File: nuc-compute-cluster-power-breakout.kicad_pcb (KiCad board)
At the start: 4 copper layers, 100 x 100 mm, 112 parts, among them J1 USB3106-30-0230-A, J2 BM04B-SRSS-TB-LF-SN, J3 BM04B-SRSS-TB-LF-SN, J4 43045-1013, J5 430450812, J6 430450812, J7 430450812, J8 430450812, J9 430450812, Q1 SQS401EN-T1_BE3, Q10 SSM3K15ACT, Q2 SQS401EN-T1_BE3, Q3 SSM3K15ACT, Q4 SSM3K15ACT, Q5 SQS401EN-T1_BE3, Q6 SSM3K15ACT, Q7 SQS401EN-T1_BE3, Q8 SQS401EN-T1_BE3, Q9 SSM3K15ACT, U1 FT2232HL-REEL, U10 TCA9534, U11 TMCS1100A2-Q1, U12 TMCS1100A2-Q1, U13 TMCS1100A2-Q1, U14 ADS7828, U15 AP62301WU-7, U7 AP62301WU-7, U8 TMCS1100A2-Q1, U9 TMCS1100A2-Q1, Y1 KX-7_12,MHz

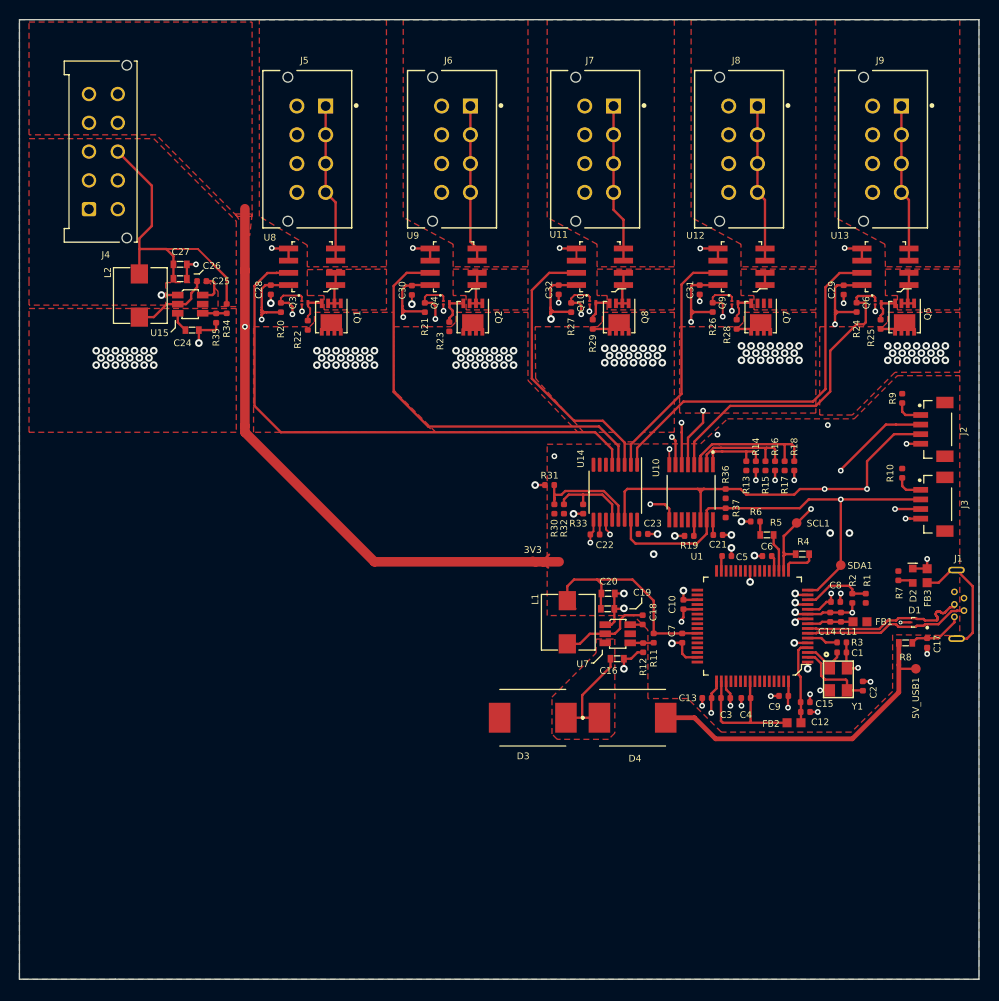
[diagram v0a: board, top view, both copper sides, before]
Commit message: Power planes alignment
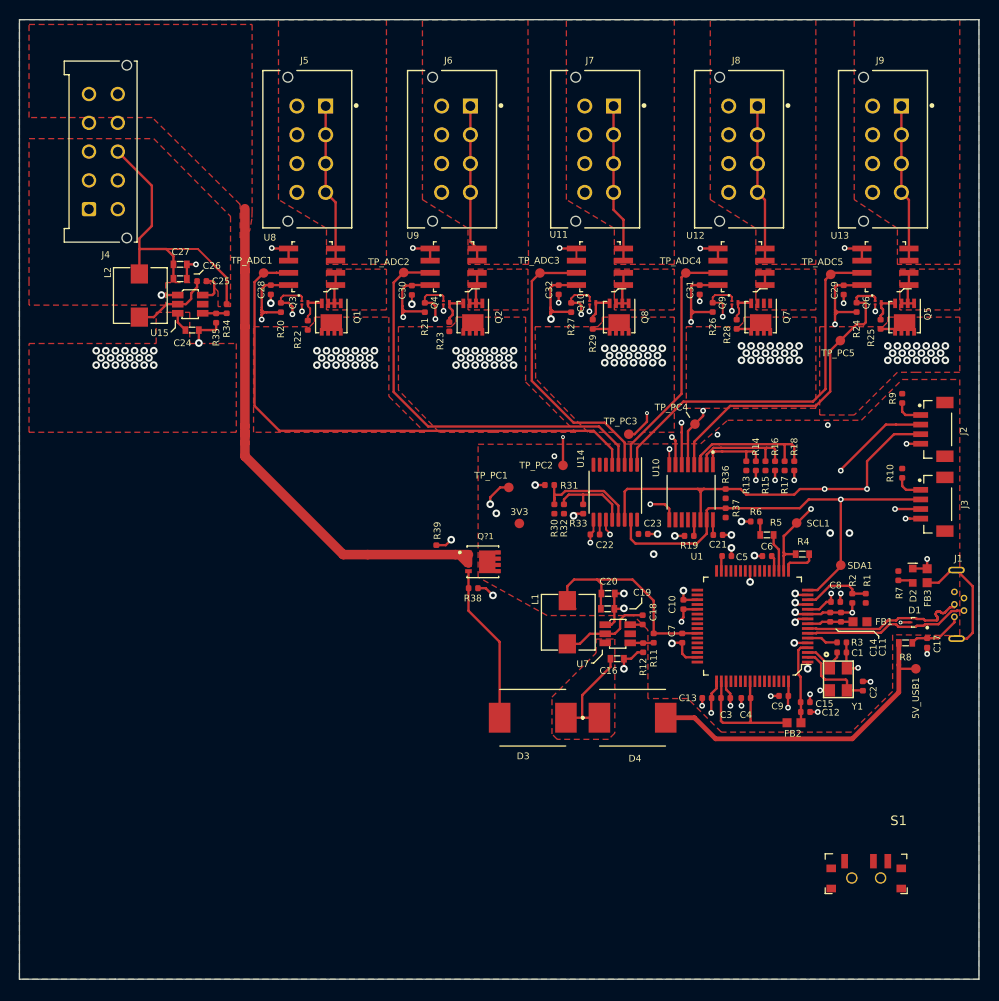
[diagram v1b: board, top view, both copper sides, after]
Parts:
- added Q?1: DMN4010LFG-7, antmicro-footprints:POWERVDFN-8, F.Cu at (138.3, 106.5)
- added R38: R_10k_0402, antmicro-footprints:0402-res, F.Cu at (137.3, 109.2)
- added R39: R_10k_0402, antmicro-footprints:0402-res, F.Cu at (133.4, 105.2)
- added S1: MSS3-V-T_R, antmicro-footprints:Switch_Slide_MSS3, F.Cu at (178.2, 139.4)
- added TP_ADC1: TP_SMD1MM, antmicro-footprints:Testpoint_smd_1mm, F.Cu at (115.5, 76.5)
- added TP_ADC2: TP_SMD1MM, antmicro-footprints:Testpoint_smd_1mm, F.Cu at (130.1, 76.4)
- added TP_ADC3: TP_SMD1MM, antmicro-footprints:Testpoint_smd_1mm, F.Cu at (144.2, 76.5)
- added TP_ADC4: TP_SMD1MM, antmicro-footprints:Testpoint_smd_1mm, F.Cu at (159.4, 76.5)
- added TP_ADC5: TP_SMD1MM, antmicro-footprints:Testpoint_smd_1mm, F.Cu at (174.6, 76.6)
- added TP_PC1: TP_SMD1MM, antmicro-footprints:Testpoint_smd_1mm, F.Cu at (141.0, 98.8)
- added TP_PC2: TP_SMD1MM, antmicro-footprints:Testpoint_smd_1mm, F.Cu at (146.7, 96.5)
- added TP_PC3: TP_SMD1MM, antmicro-footprints:Testpoint_smd_1mm, F.Cu at (153.5, 93.3)
- added TP_PC4: TP_SMD1MM, antmicro-footprints:Testpoint_smd_1mm, F.Cu at (160.4, 92.2)
- added TP_PC5: TP_SMD1MM, antmicro-footprints:Testpoint_smd_1mm, F.Cu at (175.6, 83.5)
- moved 3V3 4.19 mm to (142.1, 102.6)
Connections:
- J1 pad 4: (no net) -> Net-(J1-Pad4)
- J4 pad 10: VCC3V3 -> DB_3V3
- J4 pad 5: VCC3V3 -> DB_3V3
- U1 pad 21: (no net) -> Net-(U1-Pad21)
- U1 pad 22: (no net) -> Net-(U1-Pad22)
- U1 pad 23: (no net) -> Net-(U1-Pad23)
- U1 pad 24: (no net) -> Net-(U1-Pad24)
- U1 pad 26: (no net) -> Net-(U1-Pad26)
- U1 pad 27: (no net) -> Net-(U1-Pad27)
- U1 pad 28: (no net) -> Net-(U1-Pad28)
- U1 pad 29: (no net) -> Net-(U1-Pad29)
- U1 pad 30: (no net) -> Net-(U1-Pad30)
- U1 pad 32: (no net) -> Net-(U1-Pad32)
- U1 pad 33: (no net) -> Net-(U1-Pad33)
- U1 pad 34: (no net) -> Net-(U1-Pad34)
- U1 pad 36: (no net) -> Net-(U1-Pad36)
- U1 pad 38: (no net) -> Net-(U1-Pad38)
- U1 pad 39: (no net) -> Net-(U1-Pad39)
- U1 pad 40: (no net) -> Net-(U1-Pad40)
- U1 pad 41: (no net) -> Net-(U1-Pad41)
- U1 pad 43: (no net) -> Net-(U1-Pad43)
- U1 pad 44: (no net) -> Net-(U1-Pad44)
- U1 pad 45: (no net) -> Net-(U1-Pad45)
- U1 pad 46: (no net) -> Net-(U1-Pad46)
- U1 pad 48: (no net) -> Net-(U1-Pad48)
- U1 pad 52: (no net) -> Net-(U1-Pad52)
- U1 pad 53: (no net) -> Net-(U1-Pad53)
- U1 pad 54: (no net) -> Net-(U1-Pad54)
- U1 pad 55: (no net) -> Net-(U1-Pad55)
- U1 pad 57: (no net) -> Net-(U1-Pad57)
- U1 pad 58: (no net) -> Net-(U1-Pad58)
- U1 pad 59: (no net) -> Net-(U1-Pad59)
- U1 pad 60: (no net) -> Net-(U1-Pad60)
- U1 pad 61: (no net) -> Net-(U1-Pad61)
- U1 pad 62: (no net) -> Net-(U1-Pad62)
- U1 pad 63: (no net) -> Net-(U1-Pad63)
- U10 pad 10: (no net) -> Net-(U10-Pad10)
- U10 pad 11: (no net) -> Net-(U10-Pad11)
- U10 pad 12: (no net) -> Net-(U10-Pad12)
- U14 pad 6: (no net) -> Net-(U14-Pad6)
- U14 pad 7: (no net) -> Net-(U14-Pad7)
- U14 pad 8: (no net) -> Net-(U14-Pad8)
- U15 pad 5: (no net) -> Net-(U15-Pad5)
- U7 pad 5: (no net) -> Net-(U7-Pad5)
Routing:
- net DB_3V3: track 0.00 -> 59.0 mm
- net VCC3V3: track 237.4 -> 209.4 mm
- net VCC12V0: track 11.3 -> 27.9 mm
- net /Power Cycling & Current Measurement/PC_1: track 63.8 -> 67.7 mm, vias 2 -> 3
- net GND: track 98.5 -> 102.2 mm, vias 59 -> 61
- net /Power Cycling & Current Measurement/PC_3: track 27.5 -> 31.0 mm, vias 2 -> 3
- net /Power Cycling & Current Measurement/PC_2: track 43.2 -> 46.1 mm, vias 2 -> 3
- net /Power Cycling & Current Measurement/C_ADC3: track 29.4 -> 30.1 mm
- added copper zone on F.Cu, net DB_3V3
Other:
- board text removed: "TODO: Improve layout of Hall-effect current Sensors ( p.39 of the datasheet)"
- board text removed: "TODO: unify the font - Use EDIT --> Edit text and graphical properties"

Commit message: Replaced +3V3 with GND plane
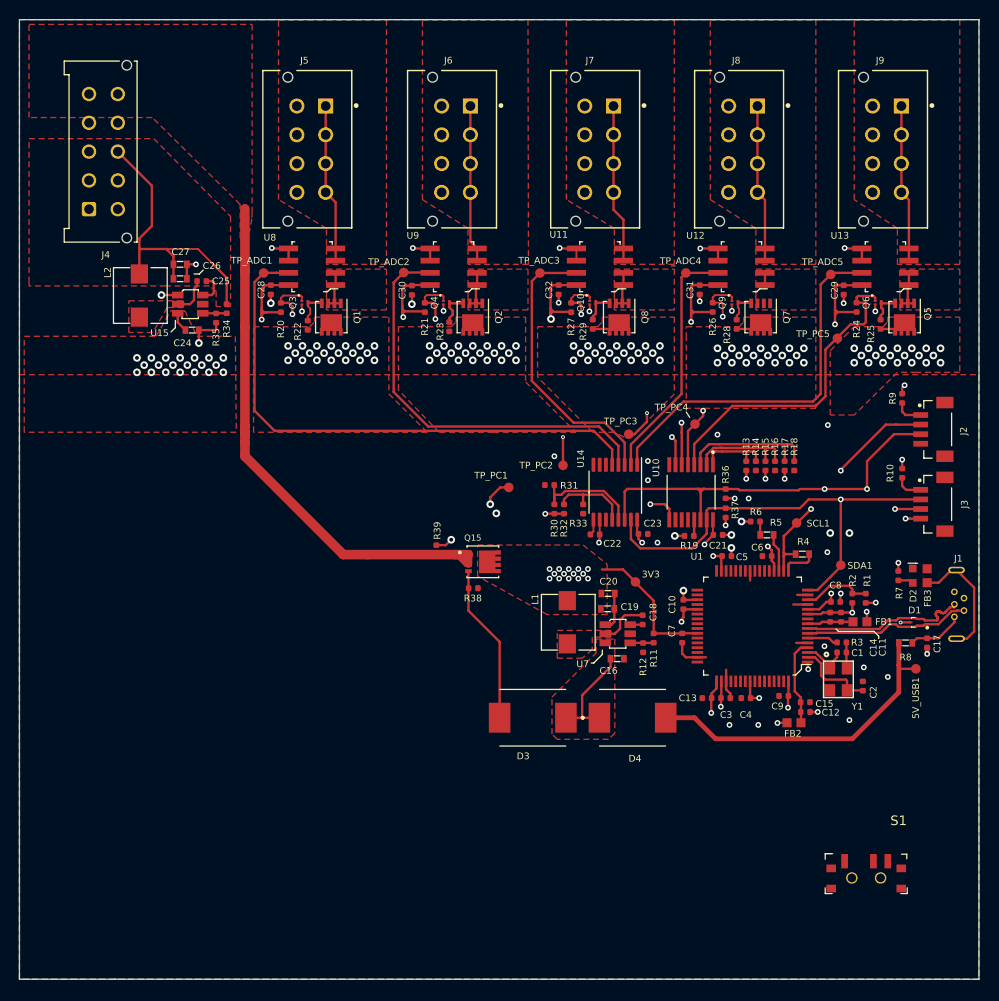
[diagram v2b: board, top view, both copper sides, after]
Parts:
- moved 3V3 13.6 mm to (154.2, 108.7)
- moved TP_PC5 0.39 mm to (175.2, 83.2)
- renumbered Q?1 to Q15
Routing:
- net GND: track 102.2 -> 70.4 mm, vias 61 -> 41
- net Net-(C18-Pad1): track 9.61 -> 5.23 mm
- net Net-(C25-Pad1): track 8.29 -> 3.98 mm
- net /Power Cycling & Current Measurement/PC_2: track 46.1 -> 49.9 mm
- net /Power Cycling & Current Measurement/PC_3: track 31.0 -> 34.8 mm
- net VCC3V3: track 209.4 -> 208.4 mm, vias 13 -> 45
- added copper zone on F.Cu, net GND
- added copper zone on F.Cu, net Net-(C18-Pad1)
- added copper zone on F.Cu, net Net-(C25-Pad1)
- added copper zone on In2.Cu, net VCC3V3
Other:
- board text removed: "TODO: Fix unequal planes distribution (TOP) -Manufacturers always require equal planes distribution on each layer."
- board text removed: "TODO: Improve layout of Net-(C18-Pad1) trace"
- board text removed: "TODO: Improve layout of Net-(C25-Pad1) trace"
- board text removed: "TODO: Increase clereances between the power planes"
- board text removed: "TODO: Move 3V3 power plane to inner layer. - Add GND plane instead"

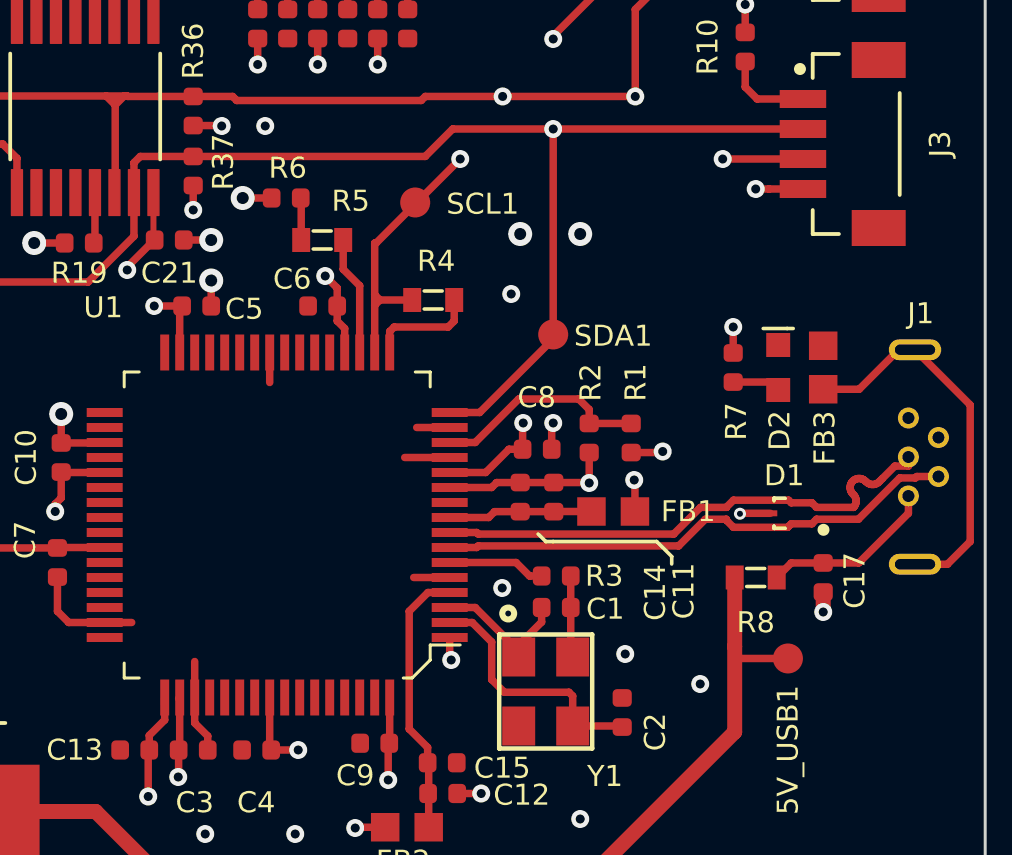
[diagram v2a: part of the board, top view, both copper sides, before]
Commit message: FTDI layout redesign
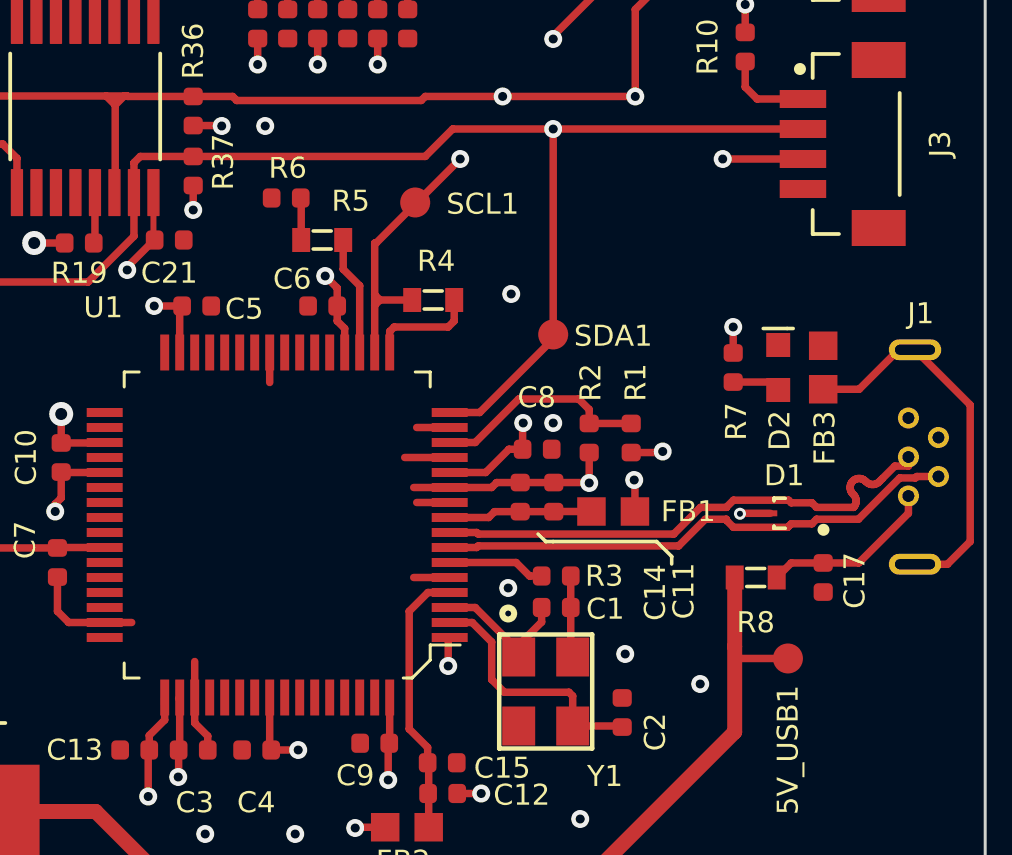
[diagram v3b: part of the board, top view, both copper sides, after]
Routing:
- net GND: track 70.4 -> 67.3 mm, vias 41 -> 36
- net VCC3V3: track 208.4 -> 206.4 mm, vias 45 -> 43
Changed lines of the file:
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@@
     (thickness 1.6)
     (drawings 22)
-    (tracks 1035)
+    (tracks 1022)
     (zones 0)
     (modules 126)
@@
   (segment (start 160.5 92) (end 160.5 93.25) (width 0.25) (layer In2.Cu) (net 1))
   (segment (start 162.75 93.25) (end 160.5 93.25) (width 0.25) (layer In2.Cu) (net 1))
-  (via (at 174.5 103.5) (size 0.8) (drill 0.4) (layers F.Cu B.Cu) (net 1))
-  (via (at 176.5 103.5) (size 0.8) (drill 0.4) (layers F.Cu B.Cu) (net 1))
-  (segment (start 174.5 103.5) (end 176.5 103.5) (width 0.5) (layer In2.Cu) (net 1))
   (segment (start 115.25 90.783172) (end 115.25 81.25) (width 0.25) (layer In2.Cu) (net 1))
   (segment (start 125.866828 101.4) (end 115.25 90.783172) (width 0.25) (layer In2.Cu) (net 1))
@@
   (segment (start 160.635 110.465) (end 160.65 110.45) (width 0.25) (layer F.Cu) (net 4))
   (segment (start 159.2 110.465) (end 160.635 110.465) (width 0.25) (layer F.Cu) (net 4))
-  (via (at 184.6 116.1) (size 0.6) (drill 0.3) (layers F.Cu B.Cu) (net 4))
-  (segment (start 184.6 115.435) (end 184.6 115.9) (width 0.5) (layer F.Cu) (net 4))
   (via (at 176.8 111.8) (size 0.6) (drill 0.3) (layers F.Cu B.Cu) (net 4))
   (segment (start 176.785 111.785) (end 176.8 111.8) (width 0.25) (layer F.Cu) (net 4))
   (segment (start 175.62 111.785) (end 176.785 111.785) (width 0.25) (layer F.Cu) (net 4))
   (segment (start 176.8 110.785) (end 176.8 111.8) (width 0.25) (layer F.Cu) (net 4))
-  (segment (start 183.925 102) (end 182.8 102) (width 0.25) (layer F.Cu) (net 4))
   (segment (start 175.9 78.65) (end 175.85 78.65) (width 0.25) (layer F.Cu) (net 4))
   (via (at 175.9 79.55) (size 0.6) (drill 0.3) (layers F.Cu B.Cu) (net 4))
@@
   (segment (start 172.4 122.15) (end 173.1 122.15) (width 0.25) (layer F.Cu) (net 4))
   (segment (start 164.2 105.9) (end 164.2 105.85) (width 0.25) (layer F.Cu) (net 4))
-  (via (at 164.2 105.05) (size 0.8) (drill 0.4) (layers F.Cu B.Cu) (net 4))
-  (segment (start 164.2 105.9) (end 164.2 105.05) (width 0.25) (layer F.Cu) (net 4))
-  (via (at 165.25 102.3) (size 0.8) (drill 0.4) (layers F.Cu B.Cu) (net 4))
-  (segment (start 166.215 102.3) (end 165.25 102.3) (width 0.25) (layer F.Cu) (net 4))
-  (via (at 182.35 102) (size 0.6) (drill 0.3) (layers F.Cu B.Cu) (net 4))
-  (segment (start 182.8 102) (end 182.35 102) (width 0.25) (layer F.Cu) (net 4))
   (segment (start 179.1825 80.3825) (end 179.2 80.4) (width 0.25) (layer F.Cu) (net 4))
   (segment (start 179.1825 80.0675) (end 179.1825 80.3825) (width 0.25) (layer F.Cu) (net 4))
@@
   (segment (start 149.825 103.325) (end 149.5 103.65) (width 0.2) (layer F.Cu) (net 4))
   (segment (start 149.825 102.1125) (end 149.825 103.325) (width 0.2) (layer F.Cu) (net 4))
-  (via (at 164.2 103.7) (size 0.8) (drill 0.4) (layers F.Cu B.Cu) (net 4))
-  (segment (start 163.285 103.7) (end 164.2 103.7) (width 0.25) (layer F.Cu) (net 4))
   (via (at 135 104.2) (size 0.8) (drill 0.4) (layers F.Cu B.Cu) (net 4))
   (segment (start 134.435 104.765) (end 135 104.2) (width 0.25) (layer F.Cu) (net 4))
@@
   (via (at 175.6 109.8) (size 0.6) (drill 0.3) (layers F.Cu B.Cu) (net 4))
   (segment (start 175.55 109.85) (end 175.6 109.8) (width 0.25) (layer F.Cu) (net 4))
-  (segment (start 175.55 110.675) (end 175.55 109.85) (width 0.25) (layer F.Cu) (net 4))
   (segment (start 160.65 116.45) (end 161.55 116.45) (width 0.25) (layer F.Cu) (net 4))
   (segment (start 163.65 118.95) (end 163.65 117.75) (width 0.25) (layer F.Cu) (net 4))
-  (via (at 172.2 117.7) (size 0.6) (drill 0.3) (layers F.Cu B.Cu) (net 4))
-  (segment (start 172.15 117.65) (end 172.2 117.7) (width 0.25) (layer F.Cu) (net 4))
-  (segment (start 172.15 116.95) (end 172.15 117.65) (width 0.25) (layer F.Cu) (net 4))
+  (via (at 172.1 117.9) (size 0.6) (drill 0.3) (layers F.Cu B.Cu) (net 4))
   (segment (start 166.15 107.45) (end 166.15 108.45) (width 0.25) (layer F.Cu) (net 4))
   (segment (start 173 115.95) (end 174.45 117.4) (width 0.25) (layer F.Cu) (net 5))
@@
   (segment (start 140.045 114.845) (end 136.8 111.6) (width 0.25) (layer F.Cu) (net 14))
   (via (at 166 99.9) (size 0.6) (drill 0.3) (layers F.Cu B.Cu) (net 4))
-  (via (at 173.9 115.3) (size 0.6) (drill 0.3) (layers F.Cu B.Cu) (net 4))
+  (via (at 174.1 115.3) (size 0.6) (drill 0.3) (layers F.Cu B.Cu) (net 4))
   (via (at 178 117.5) (size 0.6) (drill 0.3) (layers F.Cu B.Cu) (net 4))
   (via (at 180.5 118.5) (size 0.6) (drill 0.3) (layers F.Cu B.Cu) (net 4))
@@
   (via (at 155.5 96) (size 0.6) (drill 0.3) (layers F.Cu B.Cu) (net 4))
   (via (at 156.5 104.5) (size 0.6) (drill 0.3) (layers F.Cu B.Cu) (net 4))
+  (segment (start 172.1 117) (end 172.15 116.95) (width 0.25) (layer F.Cu) (net 4))
+  (segment (start 172.1 117.9) (end 172.1 117) (width 0.25) (layer F.Cu) (net 4))
+  (segment (start 172.15 112.45) (end 171.05 112.45) (width 0.25) (layer F.Cu) (net 4))
+  (segment (start 172.15 111.95) (end 170.95 111.95) (width 0.25) (layer F.Cu) (net 4))
   (segment (start 110.25 78.5) (end 110.05 78.7) (width 0.25) (layer F.Cu) (net 15))
   (segment (start 110.25 77.35) (end 110.25 78.5) (width 0.25) (layer F.Cu) (net 15))

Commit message: PCB update
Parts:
- J2, J3: value BM04B-SRSS-TB-LF-SN -> CONN_BM04B-SRSS-TB_LF__SN_
- J4: value 43045-1013 -> Conn_01x10
- Q10, Q3, Q4, Q6, Q9: value SSM3K15ACT -> SOT-883
